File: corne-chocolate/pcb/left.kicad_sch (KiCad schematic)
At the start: 79 parts, among them J1 MJ-4PP-9, J2 Conn_01x04, P1 Conn_01x01, P2 Conn_01x01, SW10 SW_PUSH, SW11 SW_PUSH, SW12 SW_PUSH, SW14 SW_PUSH, SW15 SW_PUSH, SW16 SW_PUSH, SW17 SW_PUSH, SW18 SW_PUSH, SW19 SW_PUSH, SW2 SW_PUSH, SW20 SW_PUSH, SW21 SW_PUSH, SW3 SW_PUSH, SW4 SW_PUSH, SW5 SW_PUSH, SW6 SW_PUSH, SW8 SW_PUSH, SW9 SW_PUSH, U1 ProMicro

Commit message: several important fixes
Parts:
- removed J1: MJ-4PP-9, kbd:MJ-4PP-9_1side, symbol kbd:MJ-4PP-9
- removed JP2, JP3, JP4, JP5: Device:Jumper_NO_Small, kbd:Jumper, symbol kbd:Jumper_NO_Small-Device
- removed L10, L11, L12, L14, L15, L16, L17, L18, L19, L2, L20, L21, L3, L4, L5, L6, L8, L9: SK6812MINI, kbd:YS-SK6812MINI-E, symbol kbd:SK6812MINI
- removed L22, L23, L24, L25, L26, L27: SK6812MINI, kbd:SK6812MINI_underglow_rev, symbol kbd:SK6812MINI
- removed P2: Conn_01x01, kbd:1pin_conn, symbol Connector_Generic:Conn_01x01
- added J2: 54-00174, kbd:54-00174_TEN, symbol kbd:54-00174
- added LED1, LED10, LED11, LED13, LED14, LED16, LED17, LED18, LED19, LED2, LED21, LED22, LED24, LED3, LED4, LED5, LED7, LED8: YS-SK6812MINI-E, kbd:LED_SK6812-MINI-E, symbol kbd:LED_SK6812MINI-E
- added LED12, LED15, LED20, LED23, LED6, LED9: WS2812B, kbd:LED_WS2812B_PLCC4_5.0x5.0mm_P3.2mm, symbol kbd:WS2812B
- D1: renamed from D2; item qty 100 -> (none); supplier Amazon -> Digikey; supplier pn B09DR5KFXM -> 1655-1N4148WCT-ND; vendor site https://www.amazon.com/Adafruit-Industries-1N4148-SOD-123-D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 -> (none)
- D10: renamed from D12; item qty 100 -> (none); supplier Amazon -> Digikey; supplier pn B09DR5KFXM -> 1655-1N4148WCT-ND; vendor site https://www.amazon.com/Adafruit-Industries-1N4148-SOD-123-D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 -> (none)
- D11: renamed from D14; item qty 100 -> (none); supplier Amazon -> Digikey; supplier pn B09DR5KFXM -> 1655-1N4148WCT-ND; vendor site https://www.amazon.com/Adafruit-Industries-1N4148-SOD-123-D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 -> (none)
- D12: renamed from D15; item qty 100 -> (none); supplier Amazon -> Digikey; supplier pn B09DR5KFXM -> 1655-1N4148WCT-ND; vendor site https://www.amazon.com/Adafruit-Industries-1N4148-SOD-123-D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 -> (none)
- D13: renamed from D16; item qty 100 -> (none); supplier Amazon -> Digikey; supplier pn B09DR5KFXM -> 1655-1N4148WCT-ND; vendor site https://www.amazon.com/Adafruit-Industries-1N4148-SOD-123-D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 -> (none)
- D14: renamed from D17; item qty 100 -> (none); supplier Amazon -> Digikey; supplier pn B09DR5KFXM -> 1655-1N4148WCT-ND; vendor site https://www.amazon.com/Adafruit-Industries-1N4148-SOD-123-D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 -> (none)
- D15: renamed from D18; item qty 100 -> (none); supplier Amazon -> Digikey; supplier pn B09DR5KFXM -> 1655-1N4148WCT-ND; vendor site https://www.amazon.com/Adafruit-Industries-1N4148-SOD-123-D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 -> (none)
- D16: renamed from D19; item qty 100 -> (none); supplier Amazon -> Digikey; supplier pn B09DR5KFXM -> 1655-1N4148WCT-ND; vendor site https://www.amazon.com/Adafruit-Industries-1N4148-SOD-123-D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 -> (none)
- D17: renamed from D20; item qty 100 -> (none); supplier Amazon -> Digikey; supplier pn B09DR5KFXM -> 1655-1N4148WCT-ND; vendor site https://www.amazon.com/Adafruit-Industries-1N4148-SOD-123-D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 -> (none)
- D18: renamed from D21; item qty 100 -> (none); supplier Amazon -> Digikey; supplier pn B09DR5KFXM -> 1655-1N4148WCT-ND; vendor site https://www.amazon.com/Adafruit-Industries-1N4148-SOD-123-D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 -> (none)
- D2: renamed from D3; item qty 100 -> (none); supplier Amazon -> Digikey; supplier pn B09DR5KFXM -> 1655-1N4148WCT-ND; vendor site https://www.amazon.com/Adafruit-Industries-1N4148-SOD-123-D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 -> (none)
- D3: renamed from D4; item qty 100 -> (none); supplier Amazon -> Digikey; supplier pn B09DR5KFXM -> 1655-1N4148WCT-ND; vendor site https://www.amazon.com/Adafruit-Industries-1N4148-SOD-123-D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 -> (none)
- D4: renamed from D5; item qty 100 -> (none); supplier Amazon -> Digikey; supplier pn B09DR5KFXM -> 1655-1N4148WCT-ND; vendor site https://www.amazon.com/Adafruit-Industries-1N4148-SOD-123-D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 -> (none)
- D5: renamed from D6; item qty 100 -> (none); supplier Amazon -> Digikey; supplier pn B09DR5KFXM -> 1655-1N4148WCT-ND; vendor site https://www.amazon.com/Adafruit-Industries-1N4148-SOD-123-D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 -> (none)
- D6: renamed from D8; item qty 100 -> (none); supplier Amazon -> Digikey; supplier pn B09DR5KFXM -> 1655-1N4148WCT-ND; vendor site https://www.amazon.com/Adafruit-Industries-1N4148-SOD-123-D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 -> (none)
- D7: renamed from D9; item qty 100 -> (none); supplier Amazon -> Digikey; supplier pn B09DR5KFXM -> 1655-1N4148WCT-ND; vendor site https://www.amazon.com/Adafruit-Industries-1N4148-SOD-123-D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 -> (none)
- D8: renamed from D10; item qty 100 -> (none); supplier Amazon -> Digikey; supplier pn B09DR5KFXM -> 1655-1N4148WCT-ND; vendor site https://www.amazon.com/Adafruit-Industries-1N4148-SOD-123-D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 -> (none)
- D9: renamed from D11; item qty 100 -> (none); supplier Amazon -> Digikey; supplier pn B09DR5KFXM -> 1655-1N4148WCT-ND; vendor site https://www.amazon.com/Adafruit-Industries-1N4148-SOD-123-D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 -> (none)
- J1: renamed from J2; item qty 10 -> (none); vendor site https://www.amazon.com/-/es/pantalla-pulgadas-SSD1306-contr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 -> (none)
- R1, R2: footprint kbd:R -> Resistor_SMD:R_1206_3216Metric_Pad1.30x1.75mm_HandSolder; now not fitted
- RSW1: item qty 50 -> (none); supplier Amazon -> Digikey; supplier 2 pn (none) -> B07H9ZSZD4; supplier pn B07H9ZSZD4 -> CKN12301-ND; supplier2 (none) -> Amazon; vendor site https://www.amazon.com/-/es/uxcell-0-118x0-236x0-197-Peque%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 -> (none)
- SW1: renamed from SW2; item qty 100 -> (none); supplier Amazon -> Digikey; supplier 2 pn (none) -> B0CPVJLMDJ; supplier pn B0CPVJLMDJ -> 1528-5118-ND; supplier2 (none) -> Amazon; vendor site https://www.amazon.com/100Pieces-Chocolate-Switches-Accesso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 -> (none)
- SW10: renamed from SW12; item qty 100 -> (none); supplier Amazon -> Digikey; supplier 2 pn (none) -> B0CPVJLMDJ; supplier pn B0CPVJLMDJ -> 1528-5118-ND; supplier2 (none) -> Amazon; vendor site https://www.amazon.com/100Pieces-Chocolate-Switches-Accesso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 -> (none)
- SW11: renamed from SW14; item qty 100 -> (none); supplier Amazon -> Digikey; supplier 2 pn (none) -> B0CPVJLMDJ; supplier pn B0CPVJLMDJ -> 1528-5118-ND; supplier2 (none) -> Amazon; vendor site https://www.amazon.com/100Pieces-Chocolate-Switches-Accesso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 -> (none)
- SW12: renamed from SW15; item qty 100 -> (none); supplier Amazon -> Digikey; supplier 2 pn (none) -> B0CPVJLMDJ; supplier pn B0CPVJLMDJ -> 1528-5118-ND; supplier2 (none) -> Amazon; vendor site https://www.amazon.com/100Pieces-Chocolate-Switches-Accesso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 -> (none)
- SW13: renamed from SW16; item qty 100 -> (none); supplier Amazon -> Digikey; supplier 2 pn (none) -> B0CPVJLMDJ; supplier pn B0CPVJLMDJ -> 1528-5118-ND; supplier2 (none) -> Amazon; vendor site https://www.amazon.com/100Pieces-Chocolate-Switches-Accesso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 -> (none)
- SW14: renamed from SW17; item qty 100 -> (none); supplier Amazon -> Digikey; supplier 2 pn (none) -> B0CPVJLMDJ; supplier pn B0CPVJLMDJ -> 1528-5118-ND; supplier2 (none) -> Amazon; vendor site https://www.amazon.com/100Pieces-Chocolate-Switches-Accesso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 -> (none)
- SW15: renamed from SW18; item qty 100 -> (none); supplier Amazon -> Digikey; supplier 2 pn (none) -> B0CPVJLMDJ; supplier pn B0CPVJLMDJ -> 1528-5118-ND; supplier2 (none) -> Amazon; vendor site https://www.amazon.com/100Pieces-Chocolate-Switches-Accesso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 -> (none)
- SW16: renamed from SW19; item qty 100 -> (none); supplier Amazon -> Digikey; supplier 2 pn (none) -> B0CPVJLMDJ; supplier pn B0CPVJLMDJ -> 1528-5118-ND; supplier2 (none) -> Amazon; vendor site https://www.amazon.com/100Pieces-Chocolate-Switches-Accesso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 -> (none)
- SW17: renamed from SW20; item qty 100 -> (none); supplier Amazon -> Digikey; supplier 2 pn (none) -> B0CPVJLMDJ; supplier pn B0CPVJLMDJ -> 1528-5118-ND; supplier2 (none) -> Amazon; vendor site https://www.amazon.com/100Pieces-Chocolate-Switches-Accesso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 -> (none)
- SW18: renamed from SW21; item qty 100 -> (none); supplier Amazon -> Digikey; supplier 2 pn (none) -> B0CPVJLMDJ; supplier pn B0CPVJLMDJ -> 1528-5118-ND; supplier2 (none) -> Amazon; vendor site https://www.amazon.com/100Pieces-Chocolate-Switches-Accesso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 -> (none)
- SW2: renamed from SW3; item qty 100 -> (none); supplier Amazon -> Digikey; supplier 2 pn (none) -> B0CPVJLMDJ; supplier pn B0CPVJLMDJ -> 1528-5118-ND; supplier2 (none) -> Amazon; vendor site https://www.amazon.com/100Pieces-Chocolate-Switches-Accesso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 -> (none)
- SW3: renamed from SW4; item qty 100 -> (none); supplier Amazon -> Digikey; supplier 2 pn (none) -> B0CPVJLMDJ; supplier pn B0CPVJLMDJ -> 1528-5118-ND; supplier2 (none) -> Amazon; vendor site https://www.amazon.com/100Pieces-Chocolate-Switches-Accesso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 -> (none)
- SW4: renamed from SW5; item qty 100 -> (none); supplier Amazon -> Digikey; supplier 2 pn (none) -> B0CPVJLMDJ; supplier pn B0CPVJLMDJ -> 1528-5118-ND; supplier2 (none) -> Amazon; vendor site https://www.amazon.com/100Pieces-Chocolate-Switches-Accesso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 -> (none)
- SW5: renamed from SW6; item qty 100 -> (none); supplier Amazon -> Digikey; supplier 2 pn (none) -> B0CPVJLMDJ; supplier pn B0CPVJLMDJ -> 1528-5118-ND; supplier2 (none) -> Amazon; vendor site https://www.amazon.com/100Pieces-Chocolate-Switches-Accesso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 -> (none)
- SW6: renamed from SW8; item qty 100 -> (none); supplier Amazon -> Digikey; supplier 2 pn (none) -> B0CPVJLMDJ; supplier pn B0CPVJLMDJ -> 1528-5118-ND; supplier2 (none) -> Amazon; vendor site https://www.amazon.com/100Pieces-Chocolate-Switches-Accesso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 -> (none)
- SW7: renamed from SW9; item qty 100 -> (none); supplier Amazon -> Digikey; supplier 2 pn (none) -> B0CPVJLMDJ; supplier pn B0CPVJLMDJ -> 1528-5118-ND; supplier2 (none) -> Amazon; vendor site https://www.amazon.com/100Pieces-Chocolate-Switches-Accesso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 -> (none)
- SW8: renamed from SW10; item qty 100 -> (none); supplier Amazon -> Digikey; supplier 2 pn (none) -> B0CPVJLMDJ; supplier pn B0CPVJLMDJ -> 1528-5118-ND; supplier2 (none) -> Amazon; vendor site https://www.amazon.com/100Pieces-Chocolate-Switches-Accesso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 -> (none)
- SW9: renamed from SW11; item qty 100 -> (none); supplier Amazon -> Digikey; supplier 2 pn (none) -> B0CPVJLMDJ; supplier pn B0CPVJLMDJ -> 1528-5118-ND; supplier2 (none) -> Amazon; vendor site https://www.amazon.com/100Pieces-Chocolate-Switches-Accesso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 -> (none)
- U1: item qty 3 -> (none); supplier Amazon -> Digikey; supplier 2 pn (none) -> B09TKMM8N5; supplier pn ‎B09TKMM8N5 -> 1568-1060-ND; supplier2 (none) -> Amazon; vendor site https://www.amazon.com/OSOYOO-Mega32U4-Leonardo-Module-Ardu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 -> (none)
- renumbered H5 to H3, H6 to H4, H7 to H5, H4 to H6, H3 to H7
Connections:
- net LGND: now also J1.4 (Pin_4), J2.1, LED1.3 (VSS), LED10.3 (VSS), LED11.3 (VSS), LED12.3 (VSS), LED13.3 (VSS), LED14.3 (VSS), LED15.3 (VSS), LED16.3 (VSS), LED17.3 (VSS), LED18.3 (VSS), LED19.3 (VSS), LED2.3 (VSS), LED20.3 (VSS), LED21.3 (VSS), LED22.3 (VSS), LED23.3 (VSS), LED24.3 (VSS), LED3.3 (VSS), LED4.3 (VSS), LED5.3 (VSS), LED6.3 (VSS), LED7.3 (VSS), LED8.3 (VSS), LED9.3 (VSS)
- net LLED: now also LED5.4 (DIN)
- net LSCL: now also J1.2 (Pin_2)
- net LSDA: now also J1.1 (Pin_1)
- net LVCC: now also J1.3 (Pin_3), J2.2, LED1.1 (VDD), LED10.1 (VDD), LED11.1 (VDD), LED12.1 (VDD), LED13.1 (VDD), LED14.1 (VDD), LED15.1 (VDD), LED16.1 (VDD), LED17.1 (VDD), LED18.1 (VDD), LED19.1 (VDD), LED2.1 (VDD), LED20.1 (VDD), LED21.1 (VDD), LED22.1 (VDD), LED23.1 (VDD), LED24.1 (VDD), LED3.1 (VDD), LED4.1 (VDD), LED5.1 (VDD), LED6.1 (VDD), LED7.1 (VDD), LED8.1 (VDD), LED9.1 (VDD)
- net Ldata: now also P1.1 (Pin_1), J2.4
- new net: LED22.2 (DOUT), LED23.4 (DIN)
- new net: LED21.2 (DOUT), LED22.4 (DIN)
- new net: LED11.2 (DOUT), LED12.4 (DIN)
- new net: LED10.2 (DOUT), LED11.4 (DIN)
- new net: LED18.4 (DIN), LED19.2 (DOUT)
- new net: LED13.2 (DOUT), LED19.4 (DIN)
- new net: LED4.4 (DIN), LED5.2 (DOUT)
- new net: LED1.4 (DIN), LED2.2 (DOUT)
- new net: LED2.4 (DIN), LED3.2 (DOUT)
- new net: LED10.4 (DIN), LED9.2 (DOUT)
- new net: LED8.2 (DOUT), LED9.4 (DIN)
- new net: LED6.2 (DOUT), LED7.4 (DIN)
- new net: LED1.2 (DOUT), LED6.4 (DIN)
- new net: LED15.4 (DIN), LED16.2 (DOUT)
- new net: LED16.4 (DIN), LED17.2 (DOUT)
- new net: LED17.4 (DIN), LED18.2 (DOUT)
- new net: LED7.2 (DOUT), LED8.4 (DIN)
- new net: LED14.2 (DOUT), LED20.4 (DIN)
- new net: LED14.4 (DIN), LED15.2 (DOUT)
- new net: LED23.2 (DOUT), LED24.4 (DIN)
- new net: LED3.4 (DIN), LED4.2 (DOUT)
- new net: LED12.2 (DOUT), LED13.4 (DIN)
- new net: LED20.2 (DOUT), LED21.4 (DIN)
- no-connect marks 7 -> 9

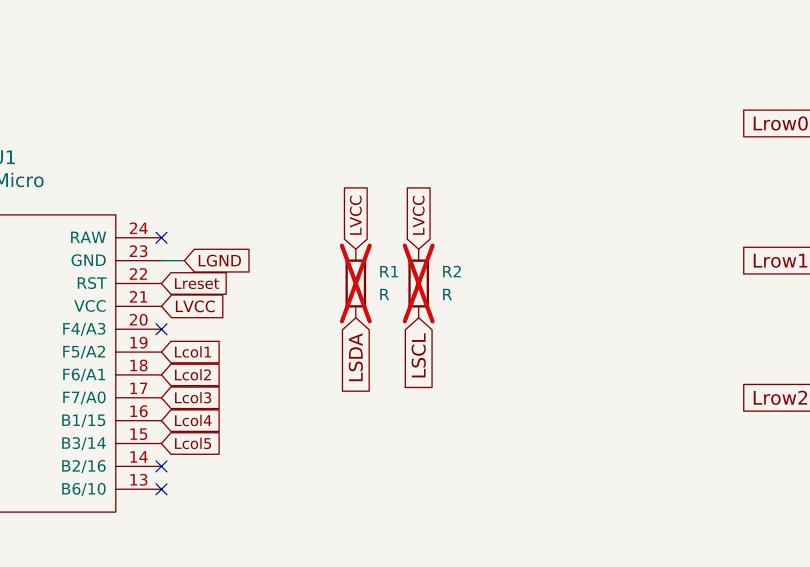
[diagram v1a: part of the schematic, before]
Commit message: zones in right keyboard
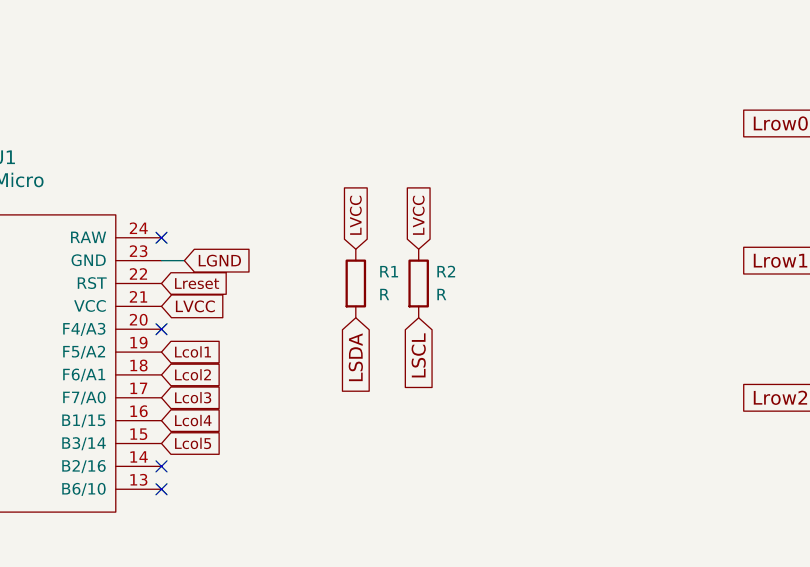
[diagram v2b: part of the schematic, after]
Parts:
- removed R1, R2: R, Resistor_SMD:R_1206_3216Metric_Pad1.30x1.75mm_HandSolder, symbol Device:R
- added R1, R2: R, kbd:R_0805_2012Metric_Pad1.20x1.40mm_HandSolder, symbol kbd:R
- H3, H4, H5, H6, H7: footprint MountingHole:MountingHole_4.3mm_M4_ISO14580 -> MountingHole:MountingHole_2.2mm_M2_ISO14580
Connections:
- net LSCL: now also R2.2
- net LSDA: now also R1.2
- net LVCC: now also R1.1, R2.1
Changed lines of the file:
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@@
       (effects (font (size 1.27 1.27)) (justify left) hide)
     )
-    (property "Footprint" "MountingHole:MountingHole_4.3mm_M4_ISO14580" (at 226.06 156.845 0)
+    (property "Footprint" "MountingHole:MountingHole_2.2mm_M2_ISO14580" (at 226.06 156.845 0)
       (effects (font (size 1.27 1.27)) hide)
     )
@@
       (effects (font (size 1.27 1.27)) (justify left) hide)
     )
-    (property "Footprint" "MountingHole:MountingHole_4.3mm_M4_ISO14580" (at 255.905 156.21 0)
+    (property "Footprint" "MountingHole:MountingHole_2.2mm_M2_ISO14580" (at 255.905 156.21 0)
       (effects (font (size 1.27 1.27)) hide)
     )
@@
     )
   )
-  (symbol (lib_id "Device:R") (at 105.41 54.61 0) (unit 1)
-    (in_bom yes) (on_board yes) (dnp yes) (fields_autoplaced)
-    (property "Reference" "R1" (at 107.95 53.34 0)
-      (effects (font (size 1.27 1.27)) (justify left))
-    )
-    (property "Value" "R" (at 107.95 55.88 0)
-      (effects (font (size 1.27 1.27)) (justify left))
-    )
-    (property "Footprint" "Resistor_SMD:R_1206_3216Metric_Pad1.30x1.75mm_HandSolder" (at 103.632 54.61 90)
-      (effects (font (size 1.27 1.27)) hide)
-    )
-    (property "Datasheet" "~" (at 105.41 54.61 0)
-      (effects (font (size 1.27 1.27)) hide)
-    )
-    (property "supplier 2 pn" "" (at 105.41 54.61 0)
-      (effects (font (size 1.27 1.27)) hide)
-    )
-    (property "supplier2" "" (at 105.41 54.61 0)
-      (effects (font (size 1.27 1.27)) hide)
-    )
-    (pin "2")
-    (pin "1")
-    (instances
-      (project "corne-chocolate"
-        (path "/b2404ab0-025a-473e-9fbb-0abc932972cf/44b7bada-24db-4130-8e14-9870ae74c889"
-          (reference "R1") (unit 1)
-        )
-      )
-    )
-  )
   (symbol (lib_id "Diode:1N4148W") (at 176.53 33.02 90) (unit 1)
     (in_bom yes) (on_board yes) (dnp no) (fields_autoplaced)
@@
         (path "/b2404ab0-025a-473e-9fbb-0abc932972cf/44b7bada-24db-4130-8e14-9870ae74c889"
           (reference "D1") (unit 1)
+        )
+      )
+    )
+  )
+  (symbol (lib_id "kbd:R") (at 112.395 54.61 0) (unit 1)
+    (in_bom yes) (on_board yes) (dnp no) (fields_autoplaced)
+    (property "Reference" "R2" (at 114.3 53.34 0)
+      (effects (font (size 1.27 1.27)) (justify left))
+    )
+    (property "Value" "R" (at 114.3 55.88 0)
+      (effects (font (size 1.27 1.27)) (justify left))
+    )
+    (property "Footprint" "kbd:R_0805_2012Metric_Pad1.20x1.40mm_HandSolder" (at 110.617 54.61 90)
+      (effects (font (size 1.27 1.27)) hide)
+    )
+    (property "Datasheet" "~" (at 112.395 54.61 0)
+      (effects (font (size 1.27 1.27)) hide)
+    )
+    (pin "2")
+    (pin "1")
+    (instances
+      (project "corne-chocolate"
+        (path "/b2404ab0-025a-473e-9fbb-0abc932972cf/44b7bada-24db-4130-8e14-9870ae74c889"
+          (reference "R2") (unit 1)
         )
       )
@@
       (effects (font (size 1.27 1.27)) (justify left) hide)
     )
-    (property "Footprint" "MountingHole:MountingHole_4.3mm_M4_ISO14580" (at 235.7138 156.8022 0)
+    (property "Footprint" "MountingHole:MountingHole_2.2mm_M2_ISO14580" (at 235.7138 156.8022 0)
       (effects (font (size 1.27 1.27)) hide)
     )
@@
     )
   )
+  (symbol (lib_id "kbd:R") (at 105.41 54.61 0) (unit 1)
+    (in_bom yes) (on_board yes) (dnp no) (fields_autoplaced)
+    (property "Reference" "R1" (at 107.95 53.34 0)
+      (effects (font (size 1.27 1.27)) (justify left))
+    )
+    (property "Value" "R" (at 107.95 55.88 0)
+      (effects (font (size 1.27 1.27)) (justify left))
+    )
+    (property "Footprint" "kbd:R_0805_2012Metric_Pad1.20x1.40mm_HandSolder" (at 103.632 54.61 90)
+      (effects (font (size 1.27 1.27)) hide)
+    )
+    (property "Datasheet" "~" (at 105.41 54.61 0)
+      (effects (font (size 1.27 1.27)) hide)
+    )
+    (pin "2")
+    (pin "1")
+    (instances
+      (project "corne-chocolate"
+        (path "/b2404ab0-025a-473e-9fbb-0abc932972cf/44b7bada-24db-4130-8e14-9870ae74c889"
+          (reference "R1") (unit 1)
+        )
+      )
+    )
+  )
   (symbol (lib_id "Connector_Generic:Conn_01x01") (at 191.77 154.305 270) (unit 1)
     (in_bom yes) (on_board yes) (dnp no)
@@
         (path "/b2404ab0-025a-473e-9fbb-0abc932972cf/44b7bada-24db-4130-8e14-9870ae74c889"
           (reference "P1") (unit 1)
-        )
-      )
-    )
-  )
-  (symbol (lib_id "Device:R") (at 112.395 54.61 0) (unit 1)
-    (in_bom yes) (on_board yes) (dnp yes) (fields_autoplaced)
-    (property "Reference" "R2" (at 114.935 53.34 0)
-      (effects (font (size 1.27 1.27)) (justify left))
-    )
-    (property "Value" "R" (at 114.935 55.88 0)
-      (effects (font (size 1.27 1.27)) (justify left))
-    )
-    (property "Footprint" "Resistor_SMD:R_1206_3216Metric_Pad1.30x1.75mm_HandSolder" (at 110.617 54.61 90)
-      (effects (font (size 1.27 1.27)) hide)
-    )
-    (property "Datasheet" "~" (at 112.395 54.61 0)
-      (effects (font (size 1.27 1.27)) hide)
-    )
-    (property "supplier 2 pn" "" (at 112.395 54.61 0)
-      (effects (font (size 1.27 1.27)) hide)
-    )
-    (property "supplier2" "" (at 112.395 54.61 0)
-      (effects (font (size 1.27 1.27)) hide)
-    )
-    (pin "2")
-    (pin "1")
-    (instances
-      (project "corne-chocolate"
-        (path "/b2404ab0-025a-473e-9fbb-0abc932972cf/44b7bada-24db-4130-8e14-9870ae74c889"
-          (reference "R2") (unit 1)
         )
       )
@@
       (effects (font (size 1.27 1.27)) (justify left) hide)
     )
-    (property "Footprint" "MountingHole:MountingHole_4.3mm_M4_ISO14580" (at 266.065 156.21 0)
+    (property "Footprint" "MountingHole:MountingHole_2.2mm_M2_ISO14580" (at 266.065 156.21 0)
       (effects (font (size 1.27 1.27)) hide)
     )
@@
       (effects (font (size 1.27 1.27)) (justify left) hide)
     )
-    (property "Footprint" "MountingHole:MountingHole_4.3mm_M4_ISO14580" (at 245.745 156.21 0)
-      (effects (font (size 1.27 1.27)) hide)
-    )
+    (property "Footprint" "MountingHole:MountingHole_2.2mm_M2_ISO14580" (at 245.745 156.21 0)
+      (effects (font (size 1.27 1.27)) hide)
+    )
